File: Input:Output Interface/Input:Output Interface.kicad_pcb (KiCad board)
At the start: 2 copper layers, 220 x 160 mm, 26 parts, among them J1 Conn_01x03_Male, J2 Conn_01x03_Male, J3 16-way-pcb-edge-Educ-8-connec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, J4 16-way-pcb-edge-Educ-8-connec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, U1 74LS37, U10 74LS01, U11 74LS04, U2 74LS04, U3 7400, U4 74LS04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

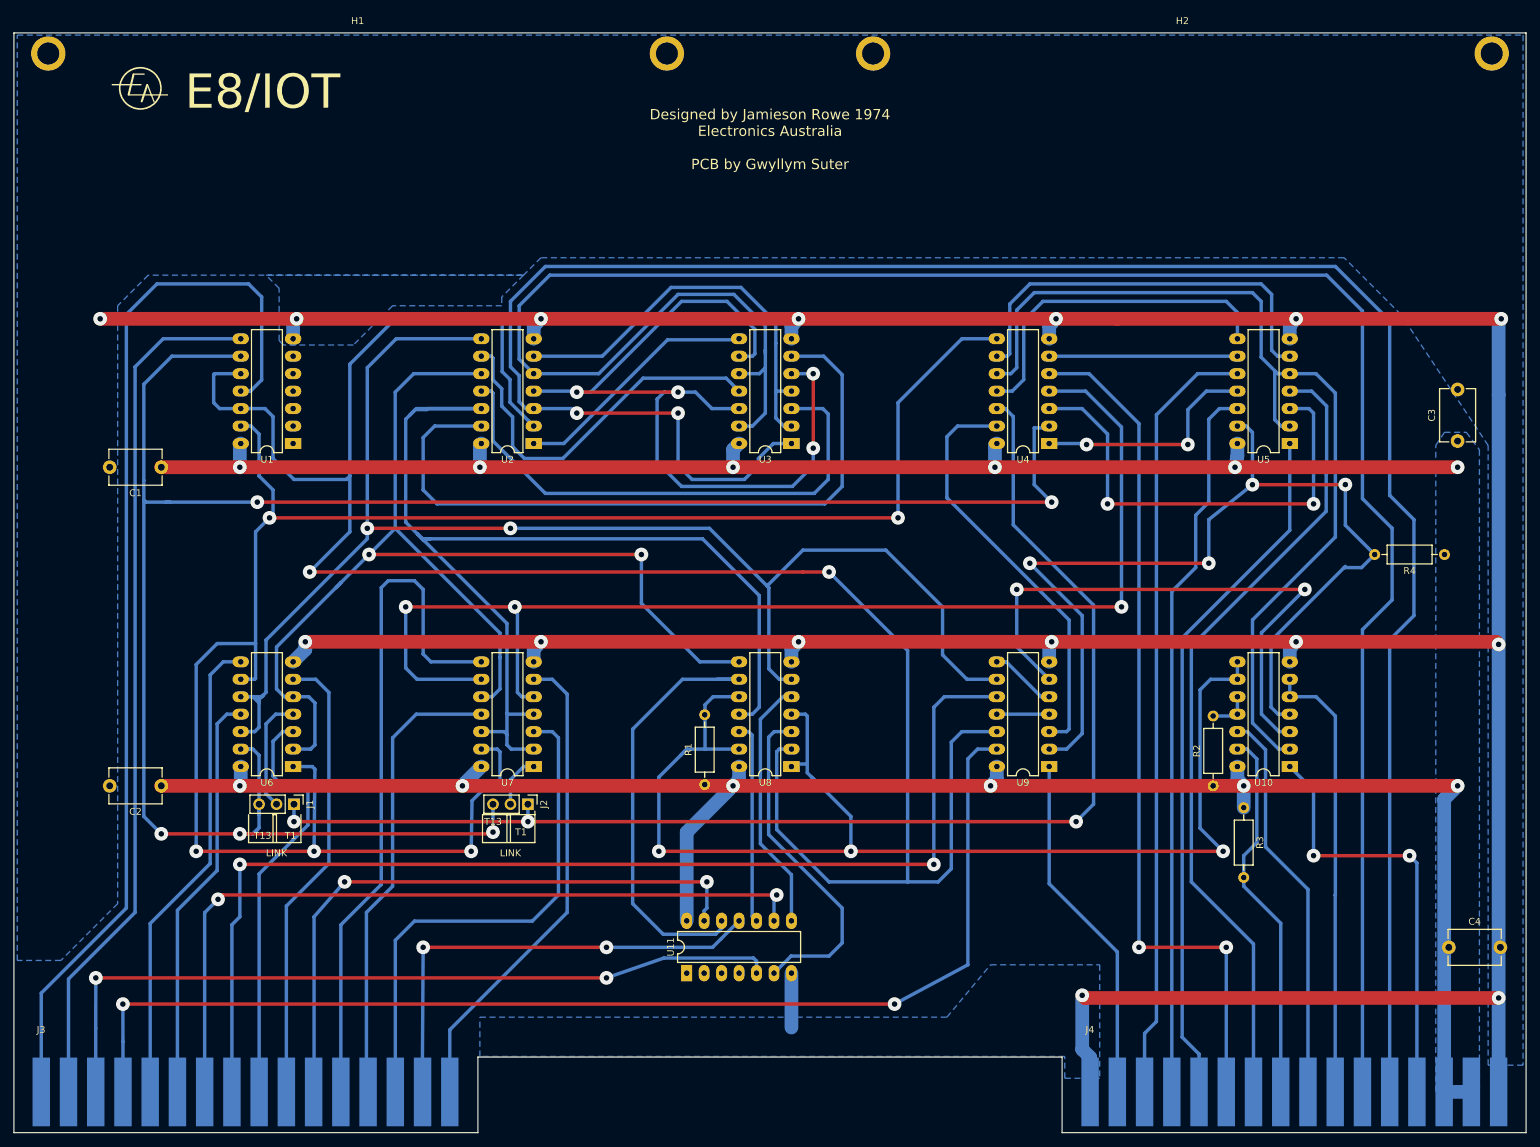
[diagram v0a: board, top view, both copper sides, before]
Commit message: Schematic update 2024-04-14 plus fixes
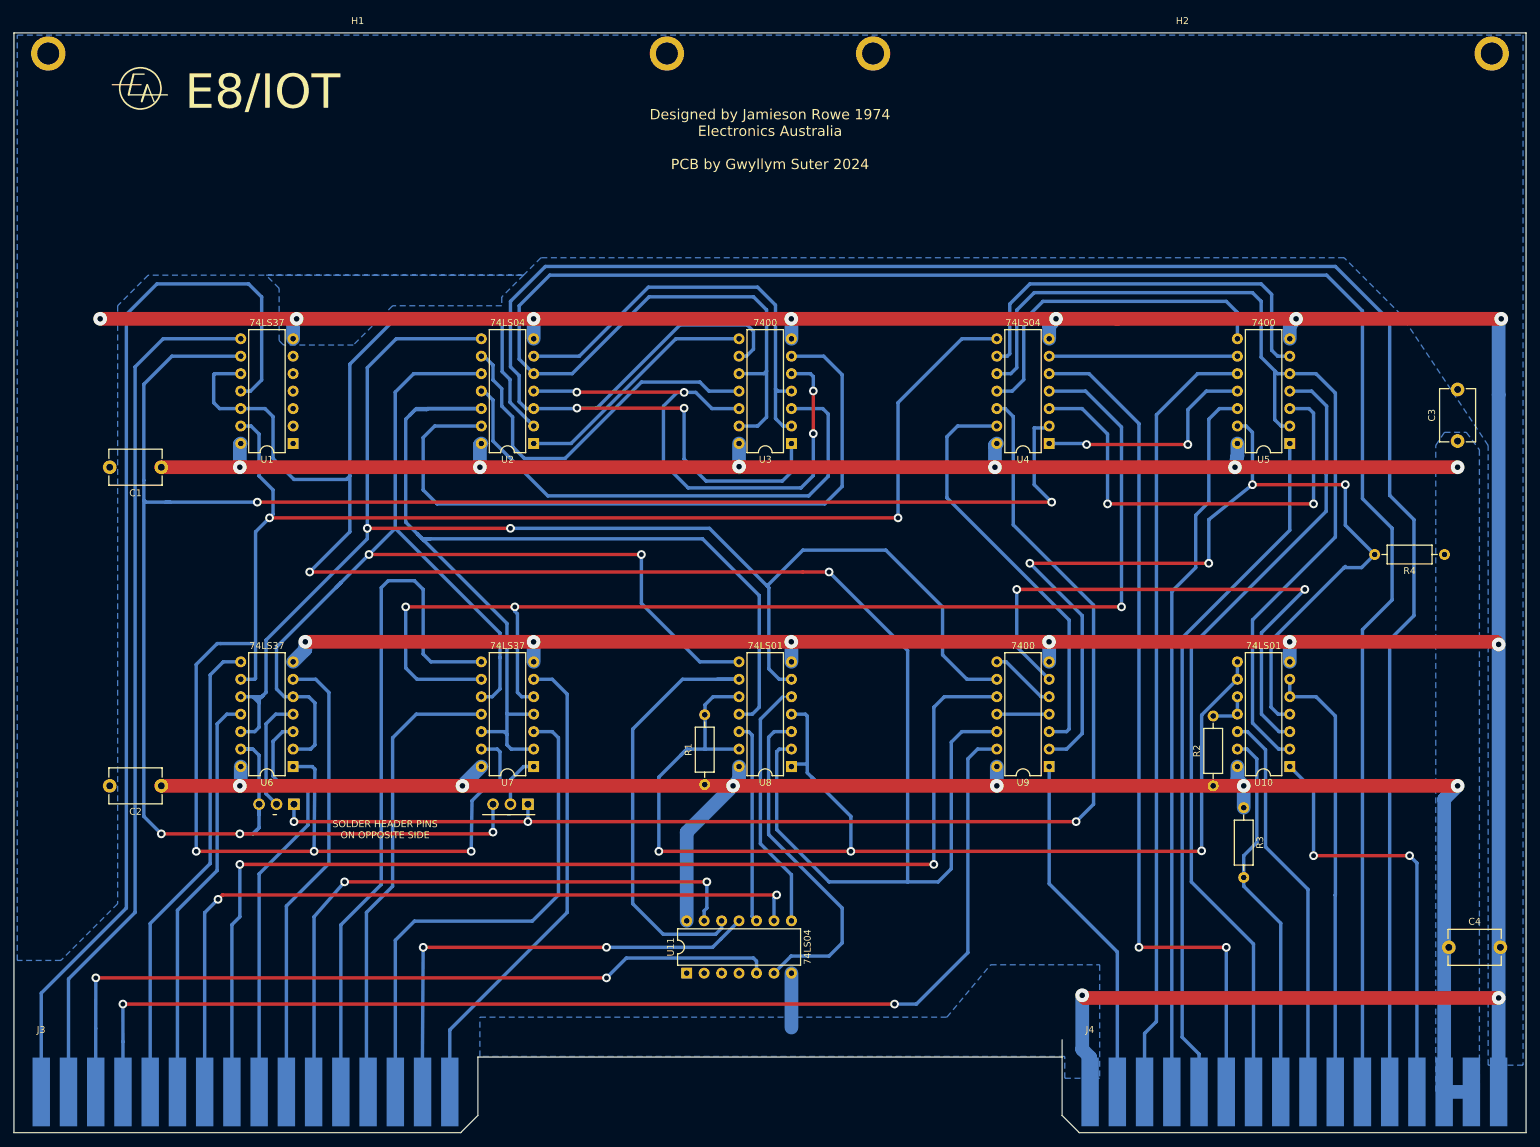
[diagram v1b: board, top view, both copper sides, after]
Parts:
- J1, J2: moved to B.Cu
- U1, U10, U11, U2, U3, U4, U5, U6, U7, U8, U9: footprint Package_DIP:DIP-14_W7.62mm_LongPads -> Package_DIP:DIP-14_W7.62mm
- turned J1 to 90 degrees
- turned J2 to 90 degrees
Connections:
- net I_D0_~CLOCK renamed I_D0_~{CLOCK}
- net I_D0_~DATA renamed I_D0_~{DATA}
- net I_D0_~FLAG renamed I_D0_~{FLAG}
- net I_D0_~FLAG_RESET renamed I_D0_~{FLAG_RESET}
- net I_D1_~CLOCK renamed I_D1_~{CLOCK}
- net I_D1_~DATA renamed I_D1_~{DATA}
- net I_D1_~FLAG renamed I_D1_~{FLAG}
- net I_D1_~FLAG_RESET renamed I_D1_~{FLAG_RESET}
- net O_D0_~CLOCK renamed O_D0_~{CLOCK}
- net O_D0_~DATA renamed O_D0_~{DATA}
- net O_D0_~FLAG renamed O_D0_~{FLAG}
- net O_D0_~FLAG_RESET renamed O_D0_~{FLAG_RESET}
- net O_D1_~CLOCK renamed O_D1_~{CLOCK}
- net O_D1_~DATA renamed O_D1_~{DATA}
- net O_D1_~FLAG renamed O_D1_~{FLAG}
- net O_D1_~FLAG_RESET renamed O_D1_~{FLAG_RESET}
- net ~CLR_IOT_FLAG renamed ~{CLR_IOT_FLAG}
- net ~IOT_SHIFT renamed ~{IOT_SHIFT}
- net ~IOT_SKIP renamed ~{IOT_SKIP}
- U1 pad 1: Net-(U1-Pad1) -> unconnected-(U1-Pad1)
- U1 pad 2: Net-(U1-Pad2) -> unconnected-(U1-Pad2)
- U1 pad 3: Net-(U1-Pad3) -> unconnected-(U1-Pad3)
- U1 pad 4: Net-(U1-Pad4) -> unconnected-(U1-Pad4)
- U1 pad 5: Net-(U1-Pad5) -> unconnected-(U1-Pad5)
- U1 pad 6: Net-(U1-Pad6) -> unconnected-(U1-Pad6)
- U3 pad 9: Net-(U2-Pad4) -> I_O_DEVICE_SELECT
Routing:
- net Net-(U2-Pad4): track 124.7 -> 84.9 mm
- net I_O_DEVICE_SELECT: track 315.1 -> 353.3 mm
- net Net-(U10-Pad8): track 182.4 -> 175.5 mm
- net GND: track 606.5 -> 604.2 mm
- net Net-(U2-Pad6): track 60.5 -> 62.1 mm
- net I_O_GATING: track 317.0 -> 318.2 mm
- net Net-(U3-Pad11): track 55.2 -> 54.1 mm
- net +5V: track 486.3 -> 485.6 mm
- net I_D0_~{FLAG}: track 115.1 -> 115.9 mm
- net Net-(U2-Pad11): track 76.8 -> 76.2 mm
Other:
- outline, holes or cut-outs redrawn
- net class Default removed
- board text added: "Designed by Jamieson Rowe 1974 Electronics Australia PCB by Gwyllym Suter 2024"
- board text added: "SOLDER HEADER PINS ON OPPOSITE SIDE"
- board text removed: "Designed by Jamieson Rowe 1974 Electronics Australia PCB by Gwyllym Suter"

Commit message: Changes 20-7-2025 E8/T. Connected 3 missing supply rail tracks to ICS Added flood fill top and bottom to reduce noise E8/F Corrected labelling on RHS board to reflect EXT_LA not GND Changed fast slow switch operation so fast is in the DOWN position. E8/C. Ran a new track to the 2 pin JST connector from EXT_LA from 10 pin connector on SR input. Added files for E8MX, 2k byte memory expansion board
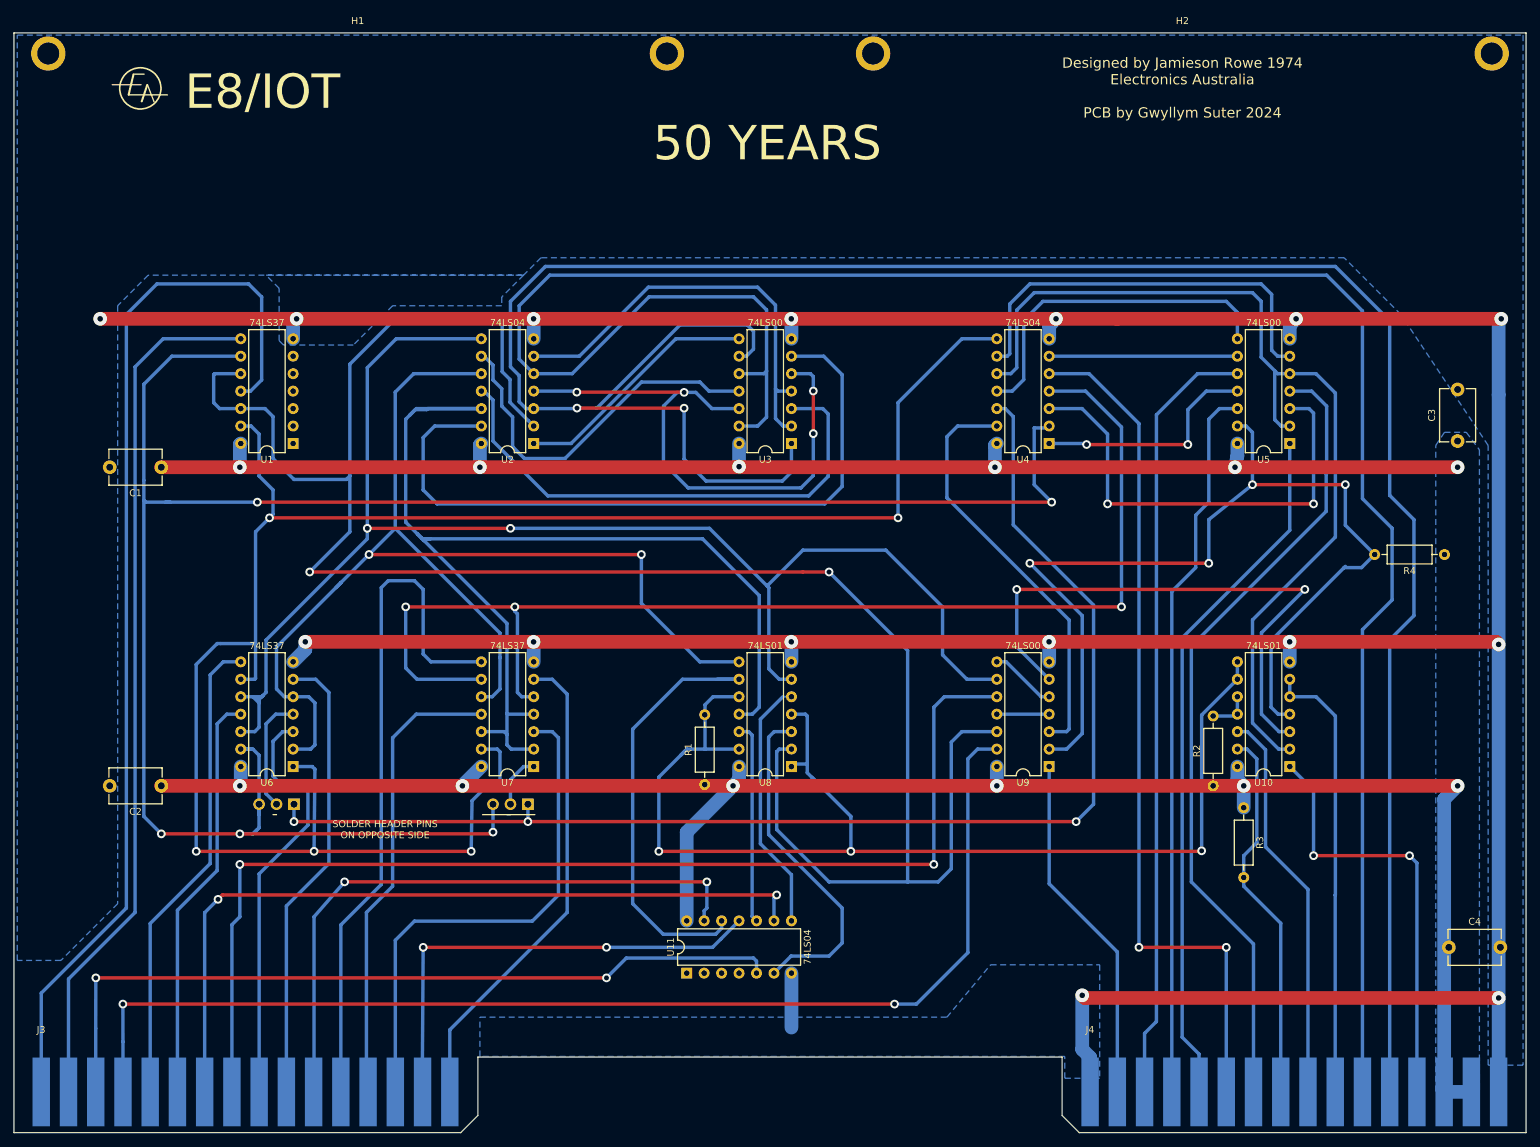
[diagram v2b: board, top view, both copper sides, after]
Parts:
- C1, C2, C3, C4: value C -> 47nF
- U3, U5, U9: value 7400 -> 74LS00
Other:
- outline, holes or cut-outs redrawn
- board text added: "50 YEARS"
